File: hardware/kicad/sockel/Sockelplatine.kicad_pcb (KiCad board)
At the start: 2 copper layers, 64 x 60 mm, 16 parts, among them J1 24V Eingang, J2 Stapelstecker 2x20, J3 Kettenstecker, Stift SMD (tre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, J4 Leistungsstecker, Stift SMD (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, U1 Raspberry Pi Pico, U2 K7805-2000R3

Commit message: Die Stifthaelften des Sockels sassen oben statt unten
Eigener Fehler aus dem Layout von gestern. J3 und J4 sind die
Stifthaelften der SMD-Steckerpaare; der Vertrag sagt "Buchse oben,
Stiftleiste unten", und der Sockel sitzt zuoberst im Stapel und treibt
nach UNTEN in das oberste Modul. Ungespiegelt auf der Oberseite zeigen
seine Stifte ins Leere, und die Pads liegen auf der falschen
Kupferlage. Aufgefallen beim Aufstellen der Bauteilliste fuer das
Motormodul -- das traegt von beiden Steckern BEIDE Haelften, und dort
faellt die Seitenfrage sofort auf.

Platz bekommt dafuer ein Feld unten; build.place() spiegelt vor dem
Vermessen des Hofes; geometry.check_all() laesst Teile auf
verschiedenen Seiten nicht mehr kollidieren -- die beiden Haelften
sitzen absichtlich am selben Ort, und wer die gemeldete "Ueberlappung"
durch Verschieben behebt, zerstoert den Stecker. Beschriftung
gespiegelter Teile wandert auf B.Fab/B.SilkS, sonst meldet die DRC
"Mirrored text on front layer".

Gate: steckerprobe prueft jetzt die Platinenseite jeder Steckerhaelfte,
aus dem Footprintnamen abgeleitet. Rot-Probe an der alten Datei: nennt
J3 und J4 einzeln.

Irrweg, festgehalten damit ihn niemand wiederholt: ich hielt es fuer
noetig, den Anker der gespiegelten Haelfte mitzuspiegeln, habe dafuer
HOF_UNTEN gebaut und wieder entfernt. Nachgerechnet ist das Gegenteil
richtig -- mit dem gewoehnlichen HOF liegen die Kontaktfelder beider
Haelften auf demselben Mittelpunkt (55,97 mm), mit dem gespiegelten
2,54 mm auseinander. KiCads Bibliothek zeichnet Buchse und Stiftleiste
bereits gespiegelt zueinander (Buchse Pad 1 rechts, Stiftleiste links),
damit sie am selben Ursprung passen.

Stand der Platine: DRC 0 Verstoesse, 0 Schaltplan-Abgleich, neun
Testreihen gruen, Steckerprobe gruen, C3 richtig gepolt, beide
Leistungsnetze 1,00 mm.

EINE offene Meldung bleibt, mit diagnostizierter Ursache: Massepin 28
des Stapelsteckers haengt an seiner eigenen Kupferinsel (3
angeschlossene Elemente statt 62 wie die an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
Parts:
- J3, J4: moved to B.Cu
- turned J3 to 180 degrees
- turned J4 to 180 degrees
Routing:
- net /GP14: track 56.9 -> 35.7 mm
- net /GP22: track 23.0 -> 14.0 mm
- net /GP10: track 31.2 -> 36.6 mm
- net 3V3: track 56.7 -> 51.6 mm
- net /PWR24V: track 67.4 -> 72.4 mm
- net /NOTAUS: track 30.3 -> 25.7 mm
- net /FLASH_RX: track 31.3 -> 27.2 mm
- net /GP16: track 30.7 -> 27.4 mm
- net /I2C_SCL: track 36.0 -> 33.2 mm, vias 0 -> 1
- net /I2C_SDA: track 37.8 -> 39.9 mm
- net /GP9: track 31.8 -> 30.1 mm, vias 2 -> 0
- net /GP15: track 51.7 -> 50.0 mm
- net /GP26: track 21.6 -> 23.0 mm
- net /GP18: track 17.0 -> 18.0 mm
- net /GP17: track 23.3 -> 23.9 mm
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
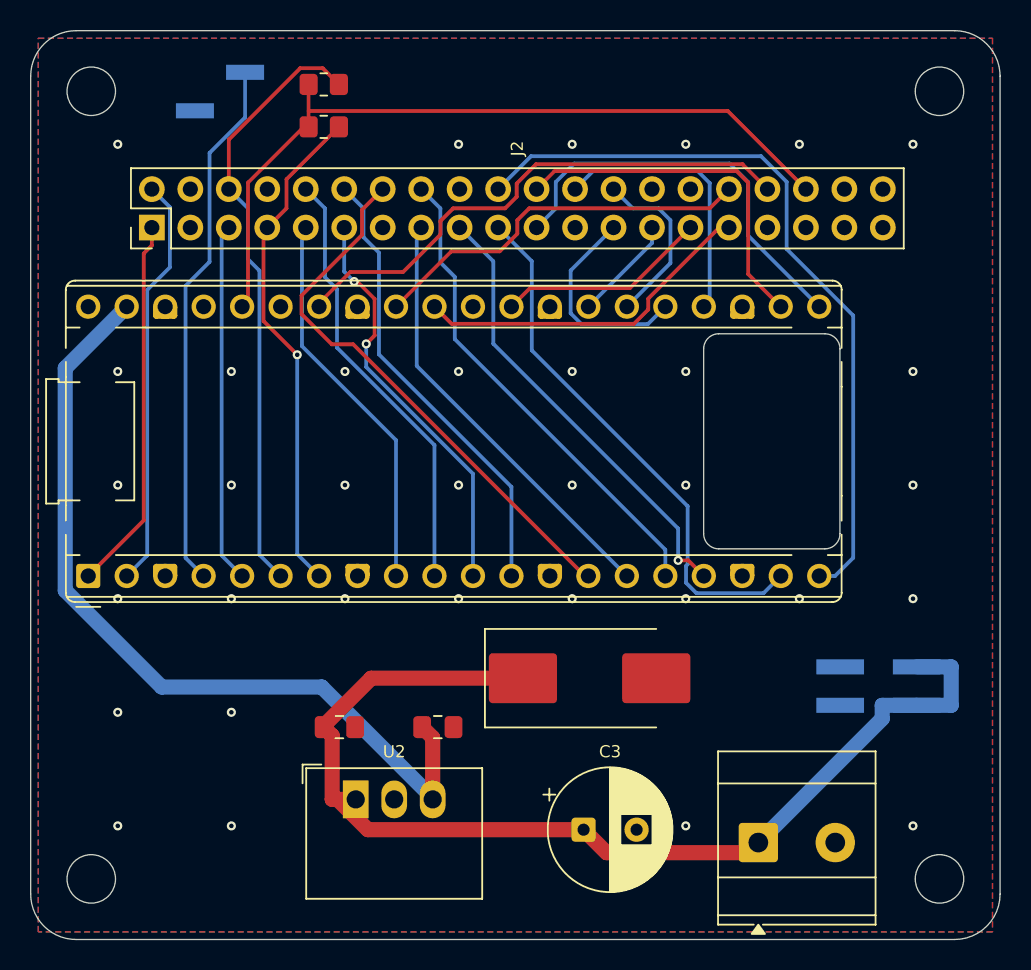
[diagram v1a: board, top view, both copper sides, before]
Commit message: GND-Vorverdrahtung: alle acht Massepins des Stapelsteckers angebunden
Der letzte offene DRC-Punkt der Sockelplatine. Unter dem Stapelstecker
zerschneiden vierzig Bahnen den Masseguss auf beiden Lagen in
eingeschlossene Inseln; in drei Router-Laeufen strandete jedes Mal ein
anderer J2-Massepin auf seiner eigenen Insel (zuletzt Pin 28 mit 3
angeschlossenen Elementen statt 62). Naehvias und kleinerer
Gussabstand halfen nachweislich nicht -- die Insel auf der Gegenlage
war ebenso eingeschlossen.

build.pre_tracks() legt jetzt VOR dem Verlegen kurze GND-Stummel von
allen acht Massepins in den freien Streifen ueber dem Stecker
(spec_sockel.PRE_TRACKS, aus dem Vertrag gerechnet statt von Hand):
freerouting kennt sie als Hindernis und fuehrt die Signalbahnen darum
herum. Alle acht Pins, nicht nur der zuletzt gestrandete -- welcher
strandet, wechselt mit jedem Lauf, das ist eine Klasse.

Geometrie nachgerechnet: obere Padreihe gerade hoch; untere Reihe hat
direkt ueber sich ein Pad derselben Spalte und bekommt einen
45-Grad-Knick auf die Spaltenmitte (Luft an den Nachbarpads 0,42 mm
gegen benoetigte 0,325). Ende bei y = 6,5, hinter der Naehvia-Reihe,
neben R1/R2, unter dem F.Cu-freien J3.

auf_platine() dedupliziert jetzt auch Segmente (0,05 mm Toleranz):
die Stummel stehen in der DSN, kommen in der SES zurueck und laegen
sonst doppelt im Kupfer -- dieselbe Falle wie bei den Naehvias.

Ergebnis, nachgemessen: DRC 0 Verstoesse / 0 offene Verbindungen / 0
Schaltplan-Abgleich, und die Masse beider Lagen ist EINE
zusammenhaengende Gruppe (vorher drei). Neun Testreihen gruen,
Steckerprobe gruen.

Co-Authored-By: Claude Opus 5 (1M context) <noreply@anthropic.com>
Claude-Session: https://claude.ai/code/session_01KDus95JJwCeRuwccgBWEi5
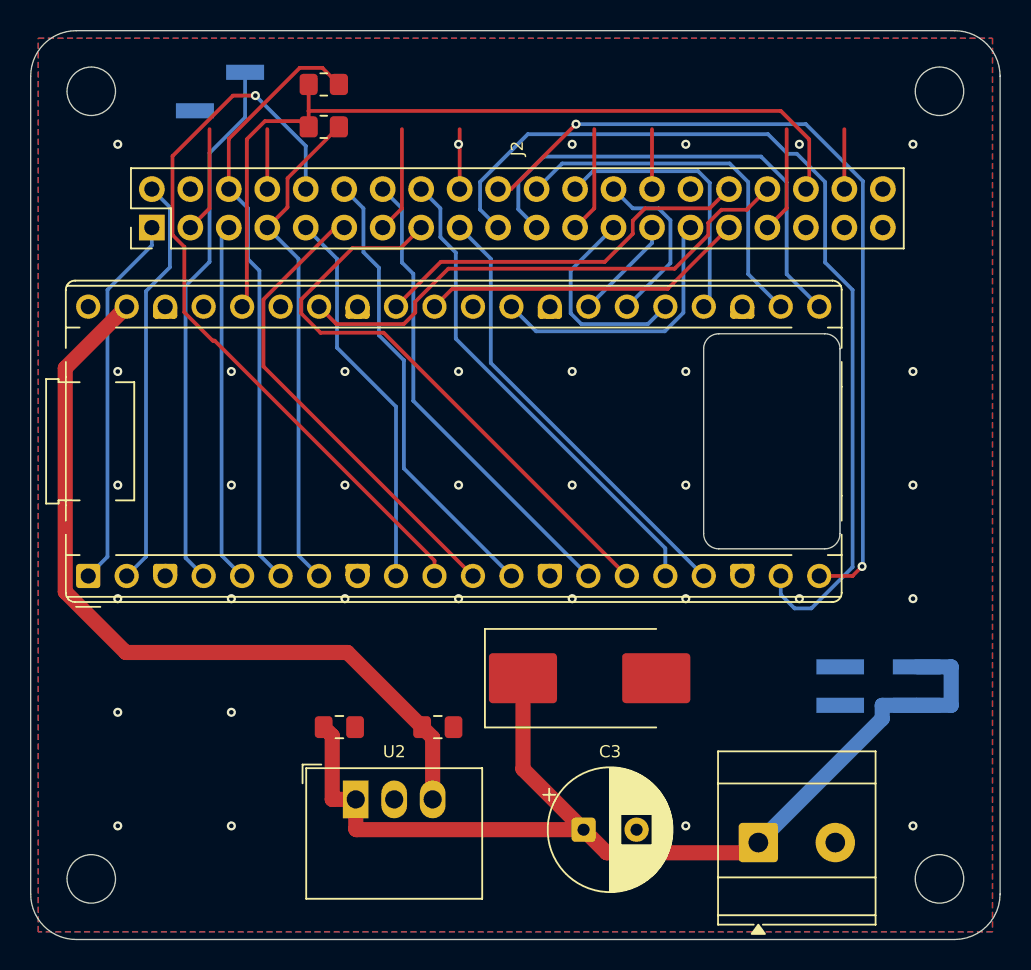
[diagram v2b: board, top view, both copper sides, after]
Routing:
- net GND: track 0.00 -> 43.9 mm
- net /GP14: track 35.7 -> 62.6 mm
- net /SEL_CLK: track 29.1 -> 49.6 mm, vias 0 -> 1
- net /GP11: track 28.9 -> 39.5 mm
- net /GP15: track 50.0 -> 56.0 mm, vias 0 -> 2
- net /GP10: track 36.6 -> 31.2 mm
- net /GP22: track 14.0 -> 18.3 mm
- net /GP16: track 27.4 -> 31.7 mm
- net 3V3: track 51.6 -> 55.9 mm
- net /GP8: track 27.1 -> 31.3 mm, vias 2 -> 0
- net /PWR24V: track 72.4 -> 69.5 mm
- net /+5V: track 55.5 -> 52.8 mm
- net /GP26: track 23.0 -> 21.6 mm
- net /GP28: track 35.3 -> 34.7 mm
- net /GP13: track 30.1 -> 29.7 mm, vias 1 -> 0
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
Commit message: Die Pflicht-Kennzeichnung des Vertrags stand auf keiner Platine
stack_spec.LAYOUT_AUFLAGEN verlangt seit Etappe 1b auf jeder Platine
ein Dreieck plus "1" neben Pin 1 des Stapelsteckers und "KLEMMEN" an
der Klemmenkante -- weil das M3-Lochbild punktsymmetrisch ist und ein
verdreht angeschraubtes Modul zwar folgenlos nicht steckt, aber ohne
Kennzeichnung niemand sieht, warum. Kein Werkzeug hat die Auflage je
umgesetzt, keine Pruefung sie angemahnt; die Sockelplatine wurde ohne
committet. Eine Auflage in Prosa, die niemand misst, ist keine.

build.kennzeichnung() setzt die Marken jetzt aus PIN1_MARKE und
KLEMMEN_POS der Platinenbeschreibung und BRICHT AB, wenn die Felder
fehlen. steckerprobe.kennzeichnungsprobe() misst an der gebauten
Platine nach (Rot-Probe: die alte Platine faellt an allen drei
Punkten durch).

Dazu die Kupferklausel derselben Auflage praezisiert, weil sie als
Flaechenregel in sich unerfuellbar war: die eigenen Loetpads des
Stapelsteckers ragen 0,17 mm in VERDREHT(leistung) hinein -- der
Vertrag verletzte seine eigene Auflage auf jeder denkbaren Platine.
Physisch druecken aber keine Flaechen, sondern Stifte, und die landen
an 46 ausrechenbaren Punkten (LANDEPUNKTE_VERDREHT(); nachgerechnet
haelt das naechste Steckerpad 1,90 mm Kupferkante Abstand). Die Regel
ist jetzt: kein freiliegendes Kupfer naeher als LANDE_SPERRRADIUS =
1,5 mm an einem Landepunkt, nur auf Modul-OBERSEITEN -- die
Sockelplatine sitzt zuoberst und ist ausdruecklich ausgenommen.
steckerprobe.verdrehtprobe() misst das an der gebauten Platine
(Pads mit Kupfer auf F.Cu plus unbedeckte Vias); alle von den
Werkzeugen gesetzten Vias sind seither ausdruecklich abgedeckt
(TENTING_MODE_TENTED), nicht der Board-Vorgabe ueberlassen.

RULING zur Zugentlastungs-Auflage: es gilt das Fuegeverfahren -- erst
stecken, dann auf die Abstandsbolzen schrauben (MONTAGE_REGEL, steht
jetzt im Vertragsdokument). Null Platinenflaeche, und nach dem
Verschrauben tragen die Bolzen jede Kraft; zusaetzliche
Befest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
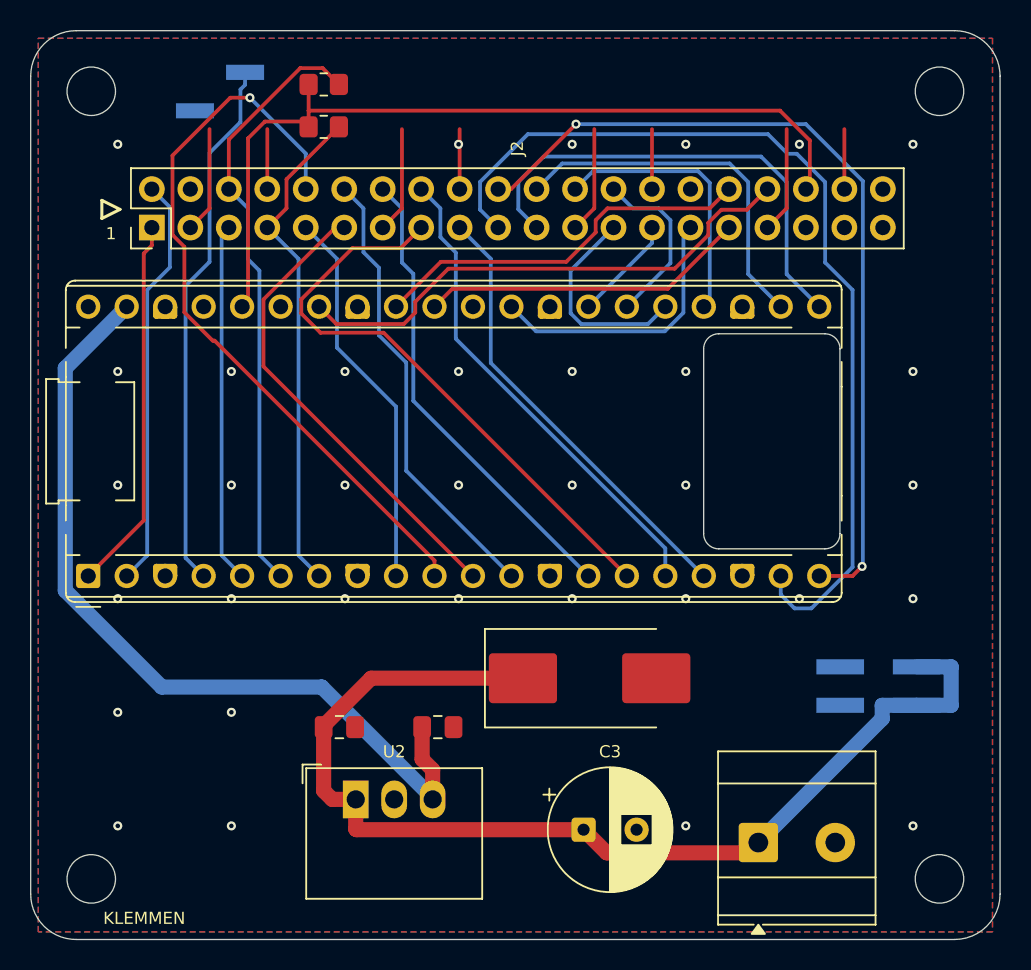
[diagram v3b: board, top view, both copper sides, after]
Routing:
- net /PWR24V: track 69.5 -> 72.4 mm
- net /+5V: track 52.8 -> 55.5 mm
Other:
- board text added: "1"
- board text added: "KLEMMEN"
